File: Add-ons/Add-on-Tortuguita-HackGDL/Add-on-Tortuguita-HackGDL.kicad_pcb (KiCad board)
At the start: 2 copper layers, 50 x 38.9 mm, 0 parts

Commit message: feat(Hw):Update_Route_And_Init_Addon_Tortuguita
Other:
- board size 50 x 38.9 mm -> 33.1 x 50 mm

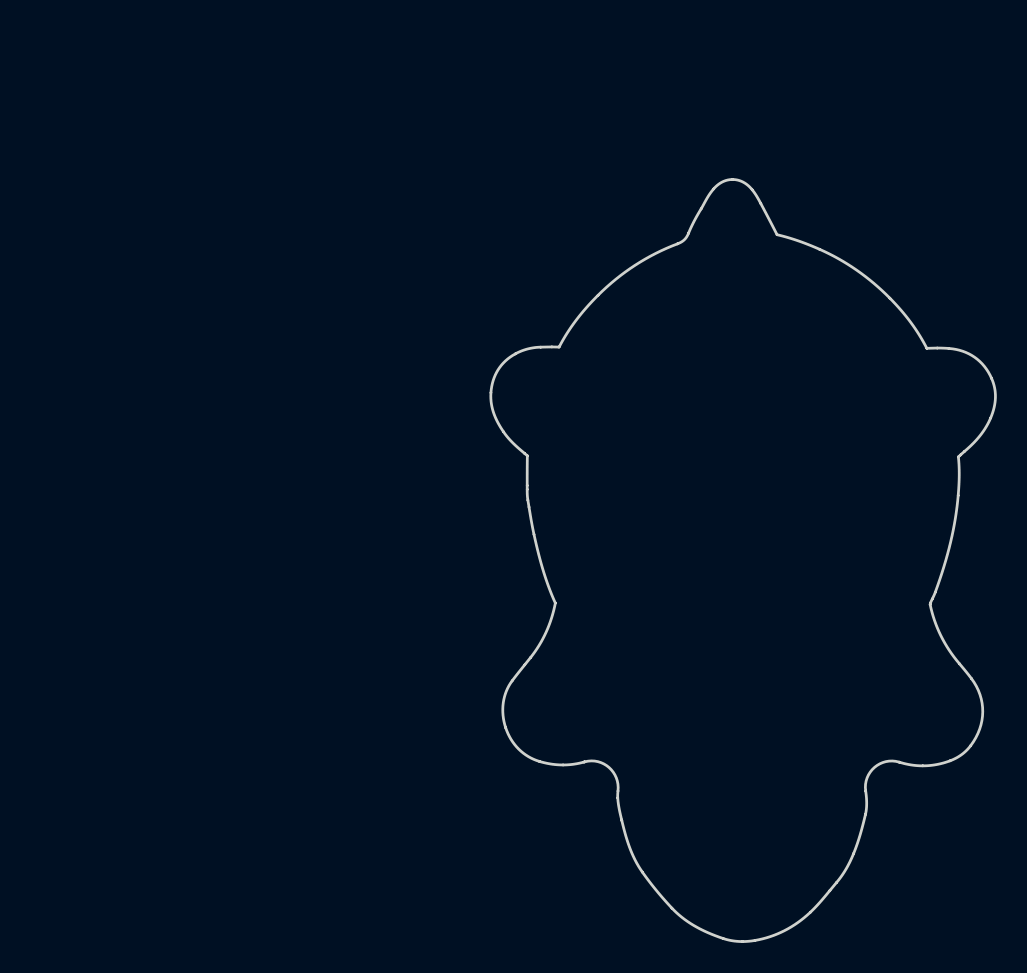
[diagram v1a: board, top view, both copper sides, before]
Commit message: feat(Hw):Update_Labels
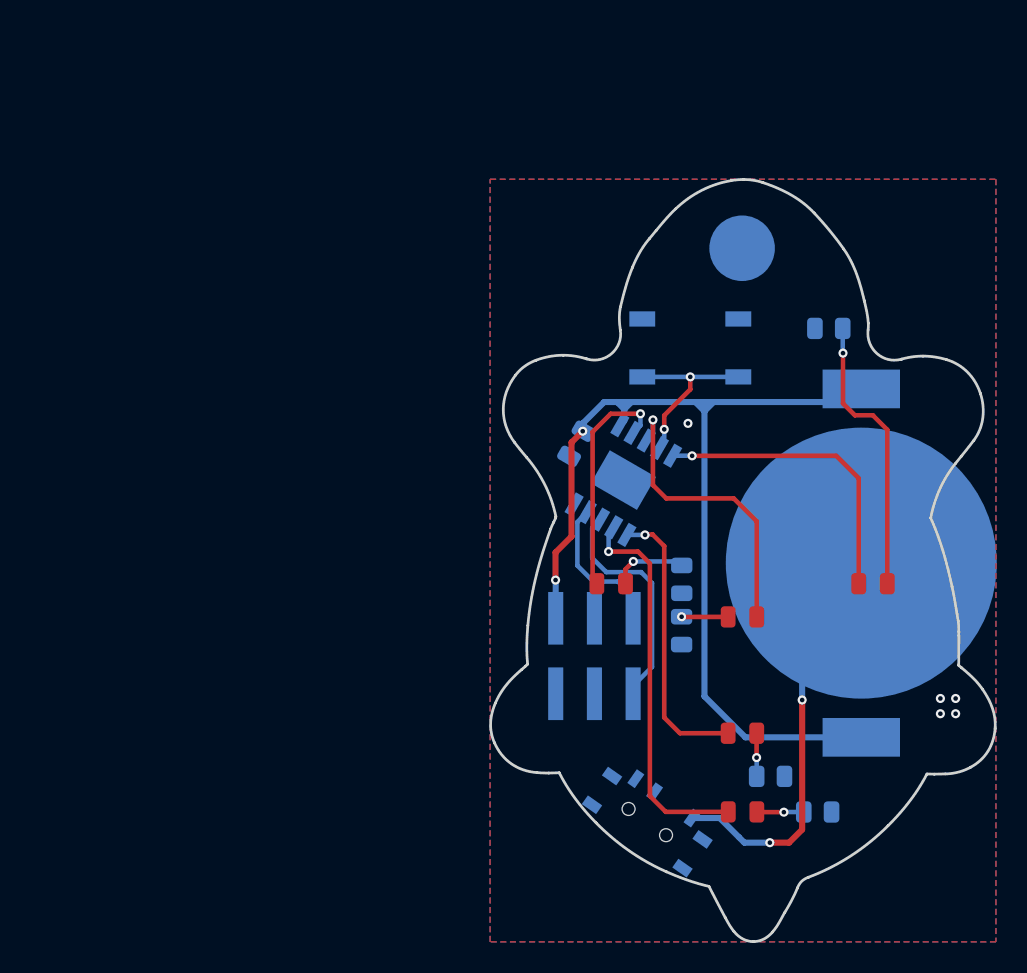
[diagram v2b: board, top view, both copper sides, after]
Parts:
- added ?: , , F.Cu at (141.0, 67.0)
- added BT1: Battery_Cell, Footprints:BAT-HLD-001, B.Cu at (148.9, 87.6)
- added C1: 0.1uF, Capacitor_SMD:C_0805_2012Metric, B.Cu at (130.2, 79.8)
- added D1: Red, LED_SMD:LED_0805_2012Metric, F.Cu at (141.1, 98.8)
- added D2: Red, LED_SMD:LED_0805_2012Metric, F.Cu at (141.1, 91.1)
- added D3: Red, LED_SMD:LED_0805_2012Metric, F.Cu at (132.4, 89.0)
- added D4: Red, LED_SMD:LED_0805_2012Metric, F.Cu at (149.6, 89.0)
- added D5: Red, LED_SMD:LED_0805_2012Metric, F.Cu at (141.1, 103.9)
- added J1: Conn_02x03_Odd_Even, Footprints:B-2100N06P-B111_CKM, B.Cu at (133.9, 96.2)
- added R1: 330R, Resistor_SMD:R_0805_2012Metric, B.Cu at (142.9, 101.6)
- added R2: 330R, Resistor_SMD:R_0805_2012Metric, B.Cu at (137.1, 92.0)
- added R3: 330R, Resistor_SMD:R_0805_2012Metric, B.Cu at (137.1, 88.7)
- added R4: 330R, Resistor_SMD:R_0805_2012Metric, B.Cu at (146.7, 72.2)
- added R5: 330R, Resistor_SMD:R_0805_2012Metric, B.Cu at (146.0, 103.9)
- added SW1: SW_RST, Button_Switch_SMD:SW_SPST_TL3342, B.Cu at (137.6, 73.5)
- added SW2: On, Footprints:MSK12C02, B.Cu at (134.8, 104.6)
- added U1: PY32F002AA15M6TU, Footprints:PY32F002AA15M, B.Cu at (133.2, 82.2)
- added kibuzzard-684B03BD: G***, kibuzzard-684B03BD, B.Cu at (140.6, 104.5)
- added kibuzzard-684B03C9: G***, kibuzzard-684B03C9, B.Cu at (137.2, 101.2)
- added kibuzzard-68929515: G***, kibuzzard-68929515, B.Cu at (134.2, 88.6)
- added kibuzzard-68929520: G***, kibuzzard-68929520, B.Cu at (129.6, 88.6)
- added kibuzzard-6892952E: G***, kibuzzard-6892952E, B.Cu at (133.9, 98.8)
- added kibuzzard-697CCF2B: G***, kibuzzard-697CCF2B, B.Cu at (128.8, 98.8)
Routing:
- net +3.3V: track 0.00 -> 68.2 mm, vias 0 -> 2
- net Net-(BT1--): track 0.00 -> 27.3 mm, vias 0 -> 2
- net /PA7: track 0.00 -> 25.6 mm, vias 0 -> 1
- net /PA5: track 0.00 -> 19.9 mm, vias 0 -> 1
- net /PA1: track 0.00 -> 19.7 mm, vias 0 -> 1
- net Net-(D4-K): track 0.00 -> 18.7 mm, vias 0 -> 1
- net /PA6: track 0.00 -> 18.6 mm, vias 0 -> 1
- net /PF0: track 0.00 -> 15.2 mm, vias 0 -> 1
- net /SWDIO: track 0.00 -> 15.1 mm
- net /NRST: track 0.00 -> 11.8 mm, vias 0 -> 2
- net /SWCLK: track 0.00 -> 9.72 mm
- net Net-(D3-K): track 0.00 -> 4.96 mm, vias 0 -> 1
- net Net-(D5-K): track 0.00 -> 3.09 mm, vias 0 -> 1
- net Net-(D2-K): track 0.00 -> 3.06 mm, vias 0 -> 1
- net Net-(D1-K): track 0.00 -> 2.84 mm, vias 0 -> 1
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- added copper zone on B.Cu, net GND
- added copper zone on F.Cu, net GND
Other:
- outline, holes or cut-outs redrawn
